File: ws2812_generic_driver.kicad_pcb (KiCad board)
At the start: 2 copper layers, 18 x 12.5 mm, 17 parts, among them J1 Conn_01x01, J2 Conn_01x01, J3 Conn_ARM_JTAG_SWD_10, J4 Conn_01x01, J5 Conn_01x01, J6 Conn_01x01, J7 Conn_01x01, U1 ATSAMD21E15L-A, U2 TC2014-3.3VxCTTR, U3 ATtiny10-TS

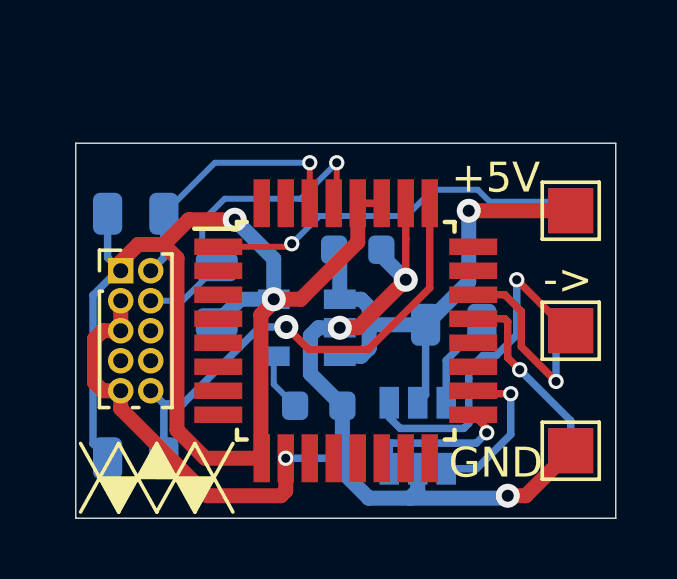
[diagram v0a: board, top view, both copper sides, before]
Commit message: Fix core overvoltage problem
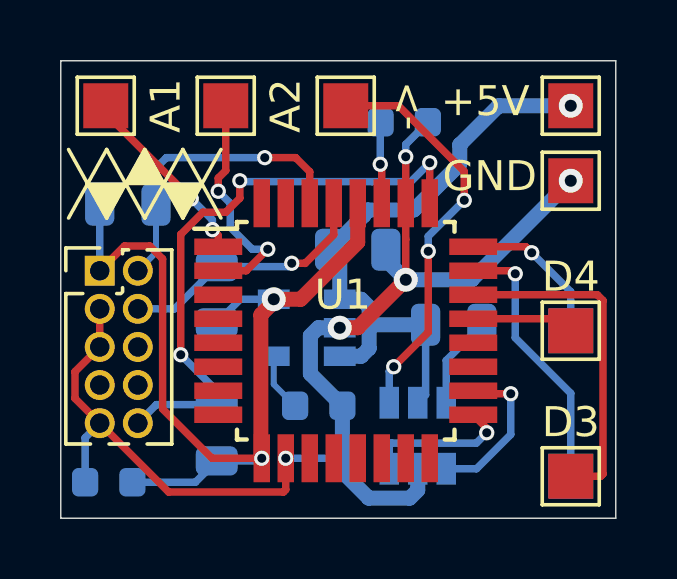
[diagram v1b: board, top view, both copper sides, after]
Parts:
- added C1: 10kpF, Capacitor_SMD:C_0603_1608Metric, B.Cu at (146.4, 97.0)
- added C2: 10kpF, Capacitor_SMD:C_0603_1608Metric, B.Cu at (136.6, 109.0)
- added J6: Conn_01x01, TestPoint:TestPoint_Pad_1.5x1.5mm, F.Cu at (152.0, 108.8)
- added J7: Conn_01x01, TestPoint:TestPoint_Pad_1.5x1.5mm, F.Cu at (152.0, 104.0)
- added J9: Conn_01x01, TestPoint:TestPoint_Pad_1.5x1.5mm, F.Cu at (140.5, 96.5)
- C3: renamed from C2; value 0.1uF -> 1uF; footprint Capacitor_SMD:C_0603_1608Metric -> Capacitor_SMD:C_0805_2012Metric
- C4: renamed from C1; value 0.01uF -> 10kpF
- J10: renamed from J3; footprint Connector_PinHeader_1.00mm:PinHeader_2x05_P1.00mm_Vertical -> Connector_PinHeader_1.27mm:PinHeader_2x05_P1.27mm_Vertical
- J8: renamed from J7; moved to F.Cu
- moved J8 15.9 mm to (136.5, 96.5)
- moved J2 10.6 mm to (144.5, 96.5)
- moved REF** 9.81 mm to (137.8, 99.1)
- moved J3 9.00 mm to (152.0, 99.0)
- moved J1 3.50 mm to (152.0, 96.5)
- moved R1 2.83 mm to (140.2, 107.4), turned to 90 degrees
- moved J5 0.85 mm to (152.0, 108.8)
- moved J10 0.70 mm to (136.3, 102.0)
- moved R3 0.40 mm to (137.2, 99.8)
- renumbered J4 to J3, J5 to J4, J6 to J5, U3 to U2, U2 to U3
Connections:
- U1 pad 2: (no net) -> A2
- U1 pad 21: D2 -> D4
- U1 pad 22: D1 -> D3
- U1 pad 23: (no net) -> D2
- U1 pad 24: (no net) -> D1
- U1 pad 27: +3.3V -> Net-(C1-Pad2)
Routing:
- net D3: track 0.00 -> 11.3 mm
- net +3.3V: track 39.8 -> 31.1 mm
- net A2: track 0.00 -> 7.82 mm, vias 0 -> 2
- net A1: track 12.8 -> 6.25 mm, vias 1 -> 2
- net GND: track 37.3 -> 43.2 mm, vias 4 -> 5
- net RESET: track 16.3 -> 20.1 mm, vias 1 -> 3
- net D4: track 0.00 -> 3.42 mm
- net Net-(C1-Pad2): track 0.00 -> 2.73 mm, vias 0 -> 1
- net +5V: track 17.7 -> 20.3 mm
- net D2: track 6.36 -> 8.96 mm
- net SWCLK: track 11.1 -> 8.76 mm
- net DOUT: track 11.6 -> 13.6 mm, vias 1 -> 3
- net D1: track 6.54 -> 5.17 mm
- net SWDIO: track 9.00 -> 10.2 mm
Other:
- board size 18 x 12.5 mm -> 18.5 x 15.2 mm
- board text added: "A1"
- board text added: "A2"
- board text added: "D3"
- board text added: "D4"
- board text added: "v0.0.2 12/06/20"
- board text removed: "A"
- board text removed: "v0.0.0 11/13/20"

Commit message: Minor fixes
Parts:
- REF**: moved to B.Cu
- moved REF** 12.6 mm to (150.3, 97.9), turned to 90 degrees
- moved C3 0.20 mm to (144.9, 101.1)
